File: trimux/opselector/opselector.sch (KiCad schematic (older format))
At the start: 36 parts, among them J1 Conn_02x05_Odd_Even, J10 Conn_01x02, J11 Conn_01x03, J12 Conn_01x03, J13 Conn_01x02, J2 Conn_02x05_Odd_Even, J3 Conn_02x05_Odd_Even, J4 Conn_01x03, J5 Conn_01x03, J6 Conn_01x03, J7 Conn_01x03, J8 Conn_01x05, J9 Conn_01x01, P1 CONN_01X03, P2 CONN_01X03, P3 CONN_01X03, SW1 SW_SPDT, U1 trimux, U2 trimux, U3 trimux, U4 trimux, U5 trimux

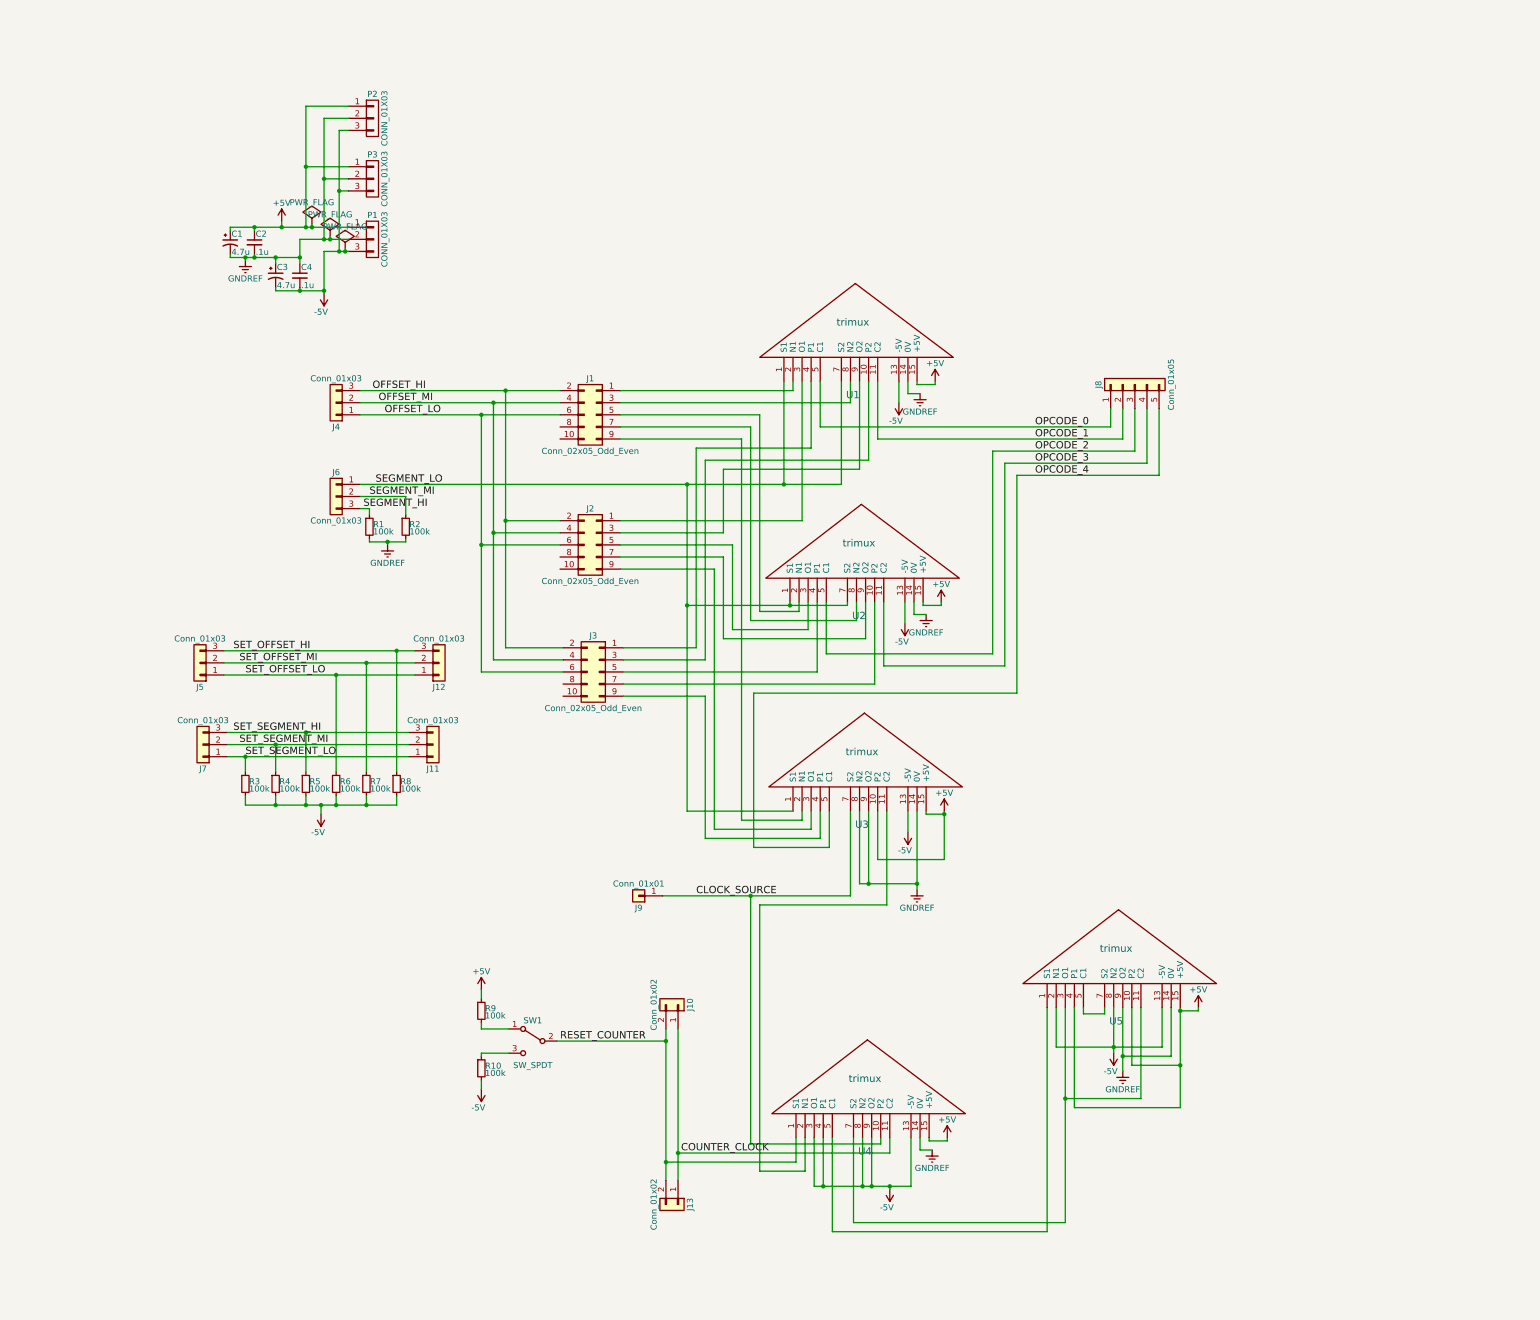
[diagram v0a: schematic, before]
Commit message: alu-a routed
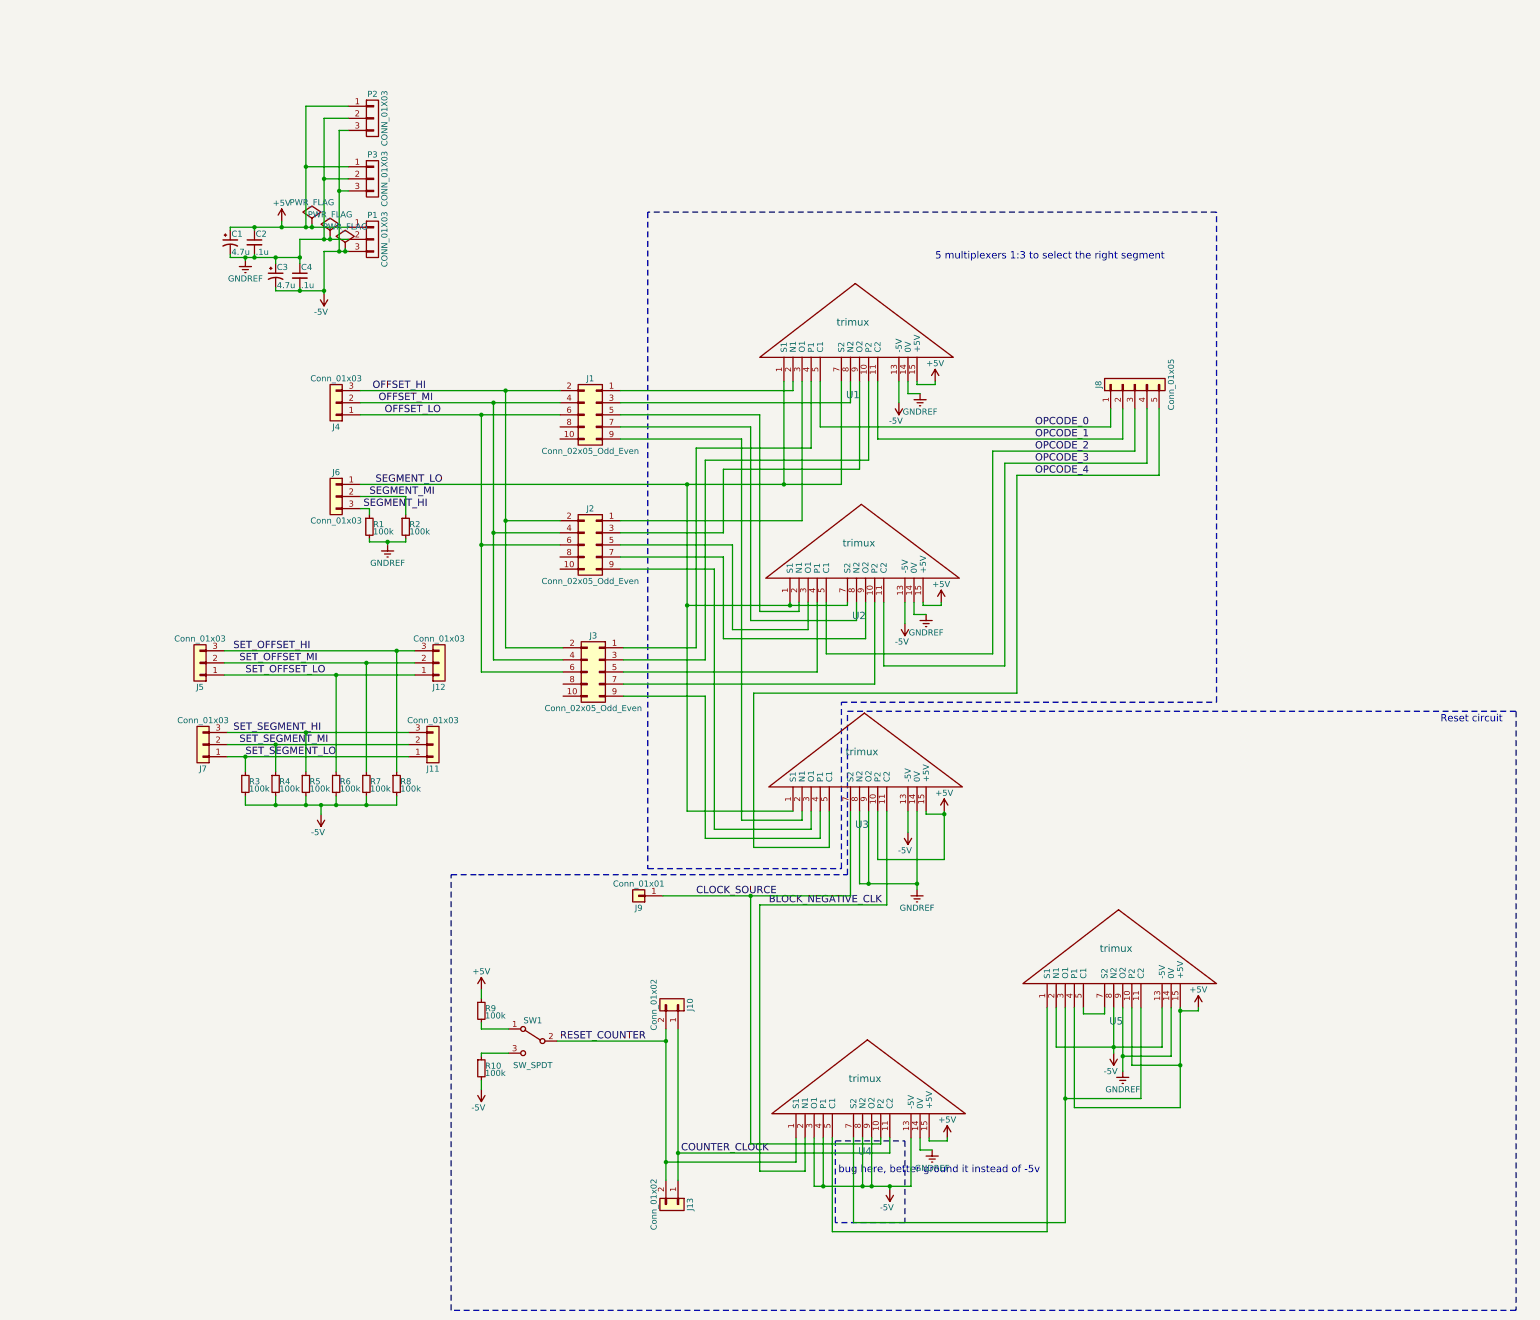
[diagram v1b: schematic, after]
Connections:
- net BLOCK_NEGATIVE_CLK: now reaches U3.11 (C2), U4.2 (N1)
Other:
- note added: "5 multiplexers 1:3 to select the right segment"
- note added: "Reset circuit"
- note added: "bug here, better ground it instead of -5v"
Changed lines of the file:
@@
 Connection ~ 1025 2275
 Connection ~ 1125 2200
+Wire Notes Line
+	875  -150 2475 -150
+Wire Notes Line
+	2475 -150 2475 -1525
+Wire Notes Line
+	2475 -1525 5575 -1525
+Wire Notes Line
+	5575 -1525 5575 -5575
+Wire Notes Line
+	5575 -5575 875  -5575
+Wire Notes Line
+	875  -5575 875  -150
+Text Notes 3250 -5175 0    60   ~ 0
+5 multiplexers 1:3 to select the right segment
+Wire Notes Line
+	-525 -100 2525 -100
+Wire Notes Line
+	2525 -100 2525 -1450
+Wire Notes Line
+	2525 -1450 8050 -1450
+Wire Notes Line
+	8050 -1450 8050 3500
+Wire Notes Line
+	8050 3500 -750 3500
+Wire Notes Line
+	-750 3500 -750 -100
+Wire Notes Line
+	-750 -100 -500 -100
+Text Notes 7425 -1350 0    60   ~ 0
+Reset circuit
+Text Label 1875 150  0    60   ~ 0
+BLOCK_NEGATIVE_CLK
+Wire Notes Line
+	2425 2100 3000 2100
+Wire Notes Line
+	3000 2100 3000 2775
+Wire Notes Line
+	3000 2775 2425 2775
+Wire Notes Line
+	2425 2775 2425 2100
+Text Notes 2450 2375 0    60   ~ 0
+bug here, better ground it instead of -5v
 $EndSCHEMATC

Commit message: opselector rerouted
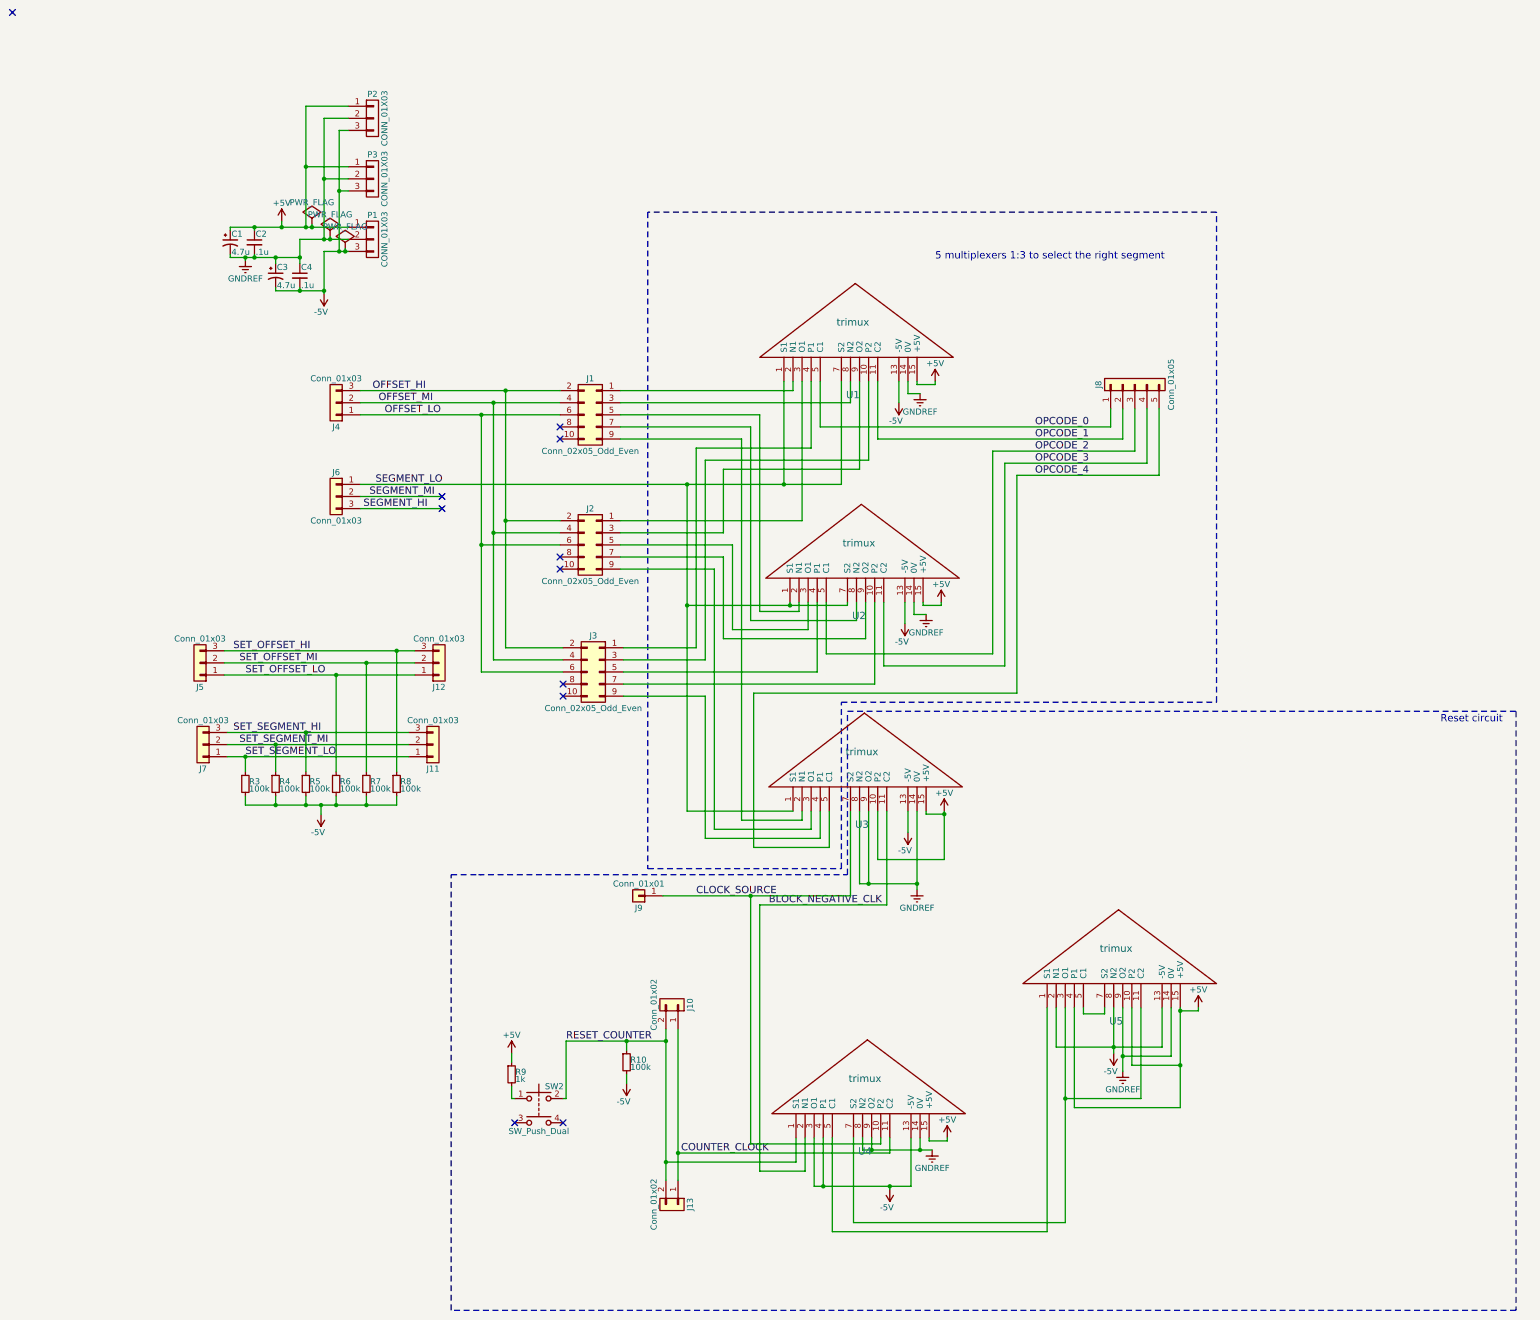
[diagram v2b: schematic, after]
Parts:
- removed R1, R2: 100k, Resistors_SMD:R_1206_HandSoldering, symbol R_Small
- removed SW1: SW_SPDT, Pin_Headers:Pin_Header_Straight_1x03_Pitch2.54mm, symbol SW_SPDT
- added SW2: SW_Push_Dual, Buttons_Switches_THT:SW_PUSH_6mm_h13mm, symbol SW_Push_Dual
- R9: value 100k -> 1k
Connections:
- net -5V: no longer U4.8 (N2), U4.9 (O2)
- net GNDREF: now also U4.8 (N2), U4.9 (O2)
- net RESET_COUNTER: now also R10.1, SW2.2
- net at R9.2: now also SW2.1
- no-connect marks 0 -> 11
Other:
- note removed: "bug here, better ground it instead of -5v"
- moved on the sheet: R10, R9
